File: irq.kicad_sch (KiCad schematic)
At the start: 7 parts, among them U1 74LS85, U11 74HCT00, U18 74LS148, U2 74HCT574, U20 74HCT574, U5 74HCT02

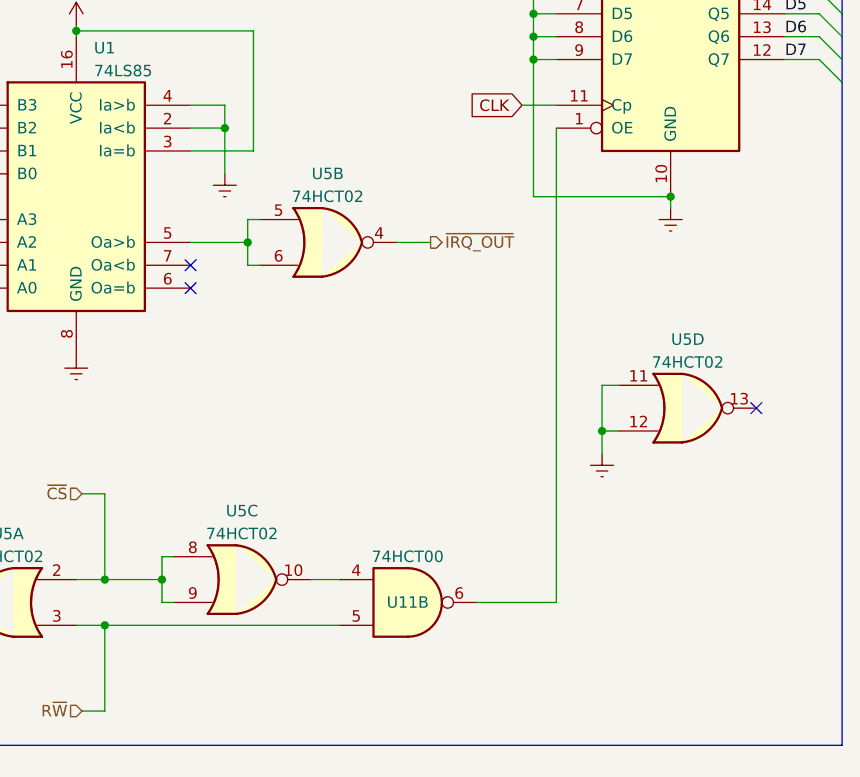
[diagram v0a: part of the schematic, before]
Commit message: fix addrdec design bug, use ca65/cmake instead of vasm/make
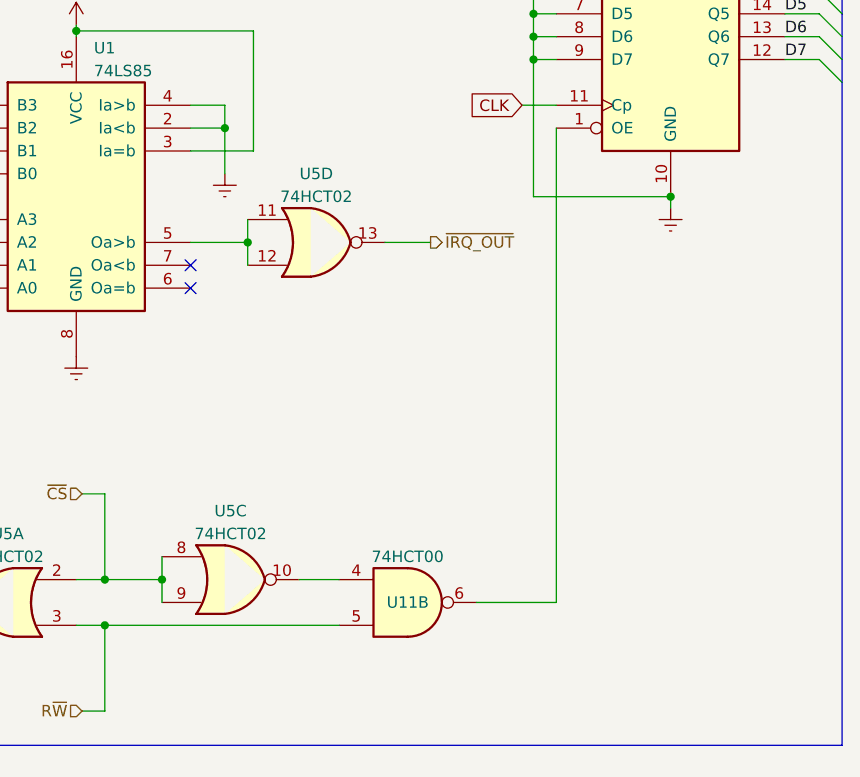
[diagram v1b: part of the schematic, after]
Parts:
- removed unit 4 of U5
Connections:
- net ~{IRQ_OUT}: now also U5.13; no longer U5.4
- new net: U1.5 (Oa>b), U5.11, U5.12
- no-connect marks 8 -> 7
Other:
- moved on the sheet: U5C, U5D

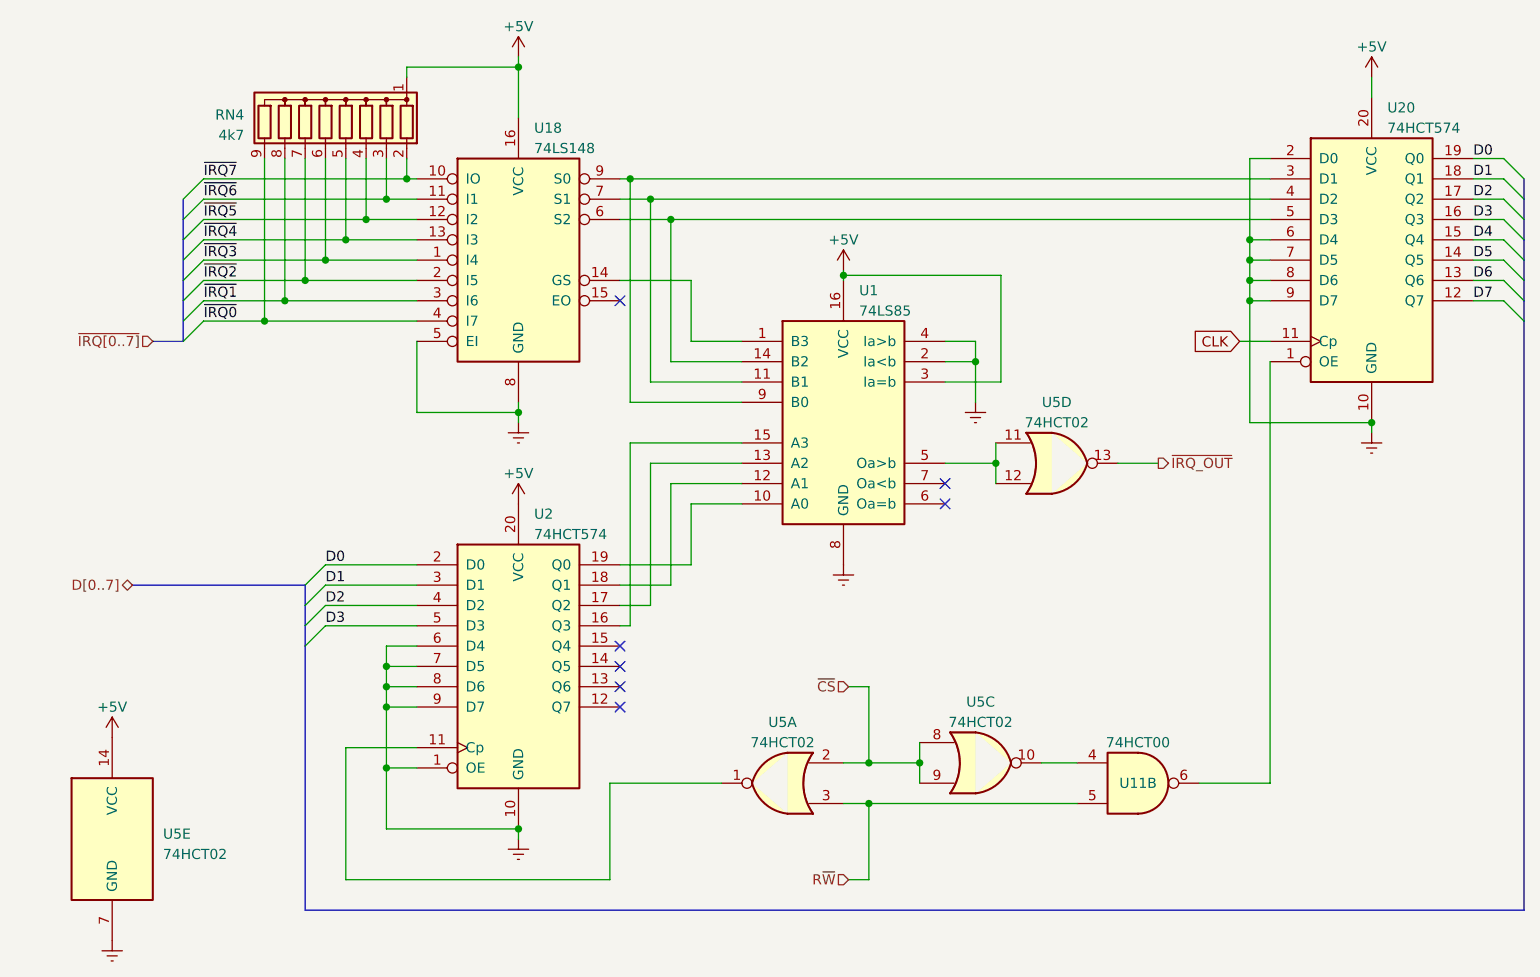
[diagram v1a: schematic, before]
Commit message: add address decoding timings
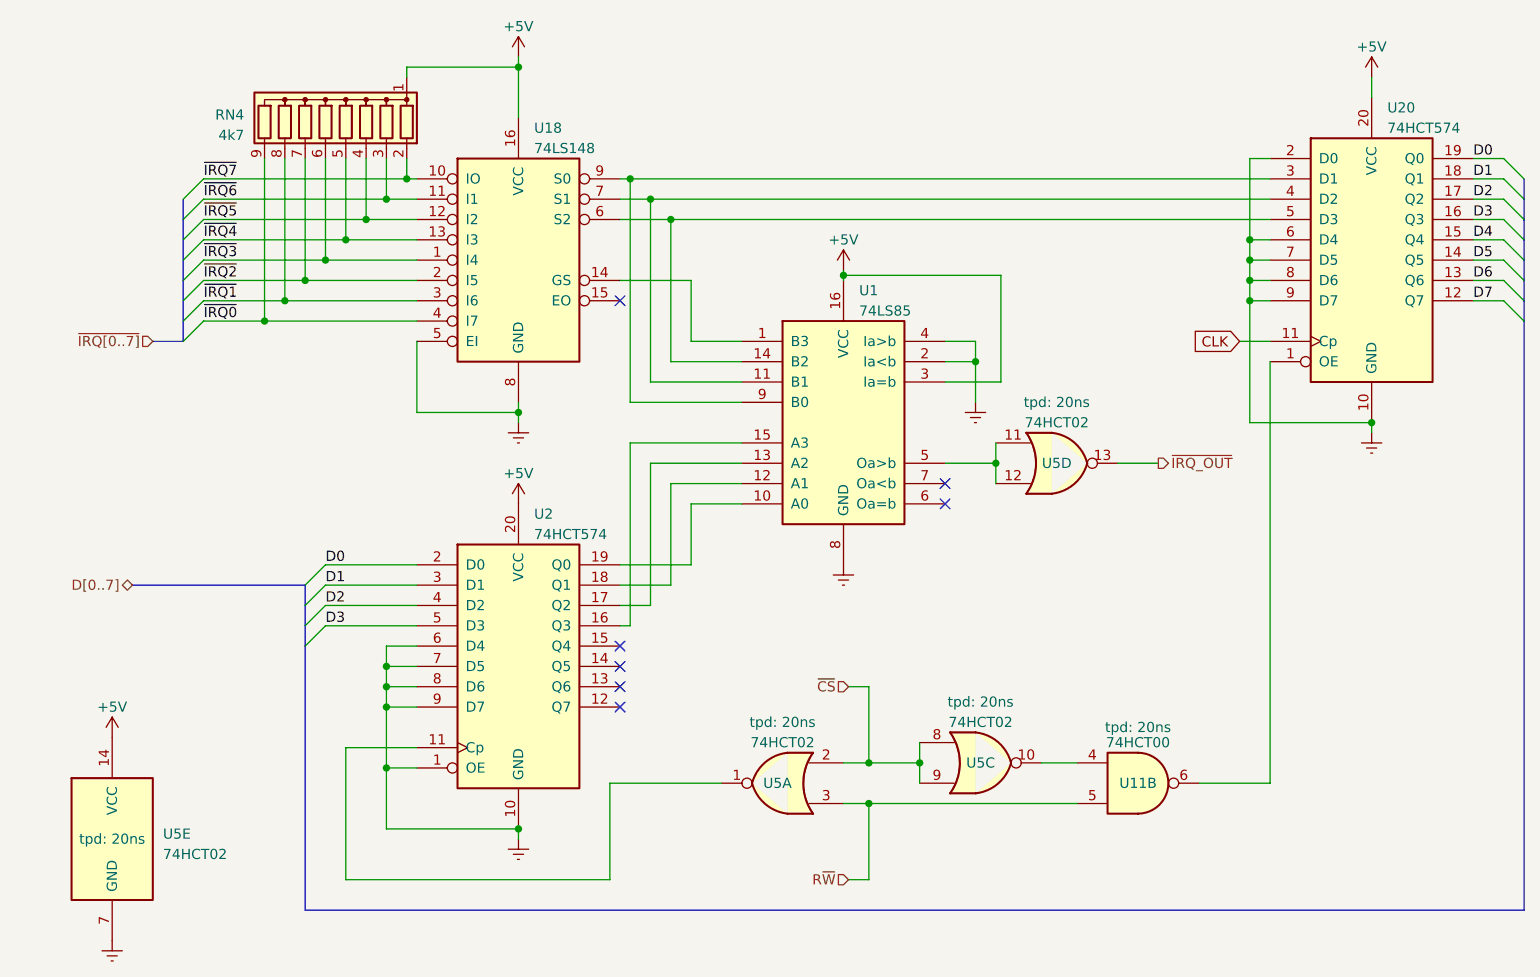
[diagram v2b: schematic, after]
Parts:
- U11, U5: tpd (none) -> 20ns
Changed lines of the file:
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@@
       (effects (font (size 1.27 1.27)) hide)
+    )
+    (property "tpd" "20ns" (at 156.21 105.41 0) (show_name)
+      (effects (font (size 1.27 1.27)))
     )
     (pin "1")
@@
   )
   (symbol (lib_id "74xx:74HCT02") (at 146.05 72.39 0) (unit 4)
-    (in_bom yes) (on_board yes) (dnp no) (fields_autoplaced)
-    (property "Reference" "U5" (at 146.05 64.77 0)
+    (in_bom yes) (on_board yes) (dnp no)
+    (property "Reference" "U5" (at 146.05 72.39 0)
       (effects (font (size 1.27 1.27)))
     )
@@
     (property "Datasheet" "http://www.ti.com/lit/gpn/sn74hct02" (at 146.05 72.39 0)
       (effects (font (size 1.27 1.27)) hide)
+    )
+    (property "tpd" "20ns" (at 146.05 64.77 0) (show_name)
+      (effects (font (size 1.27 1.27)))
     )
     (pin "1")
@@
   )
   (symbol (lib_id "74xx:74HCT02") (at 136.525 109.855 0) (unit 3)
-    (in_bom yes) (on_board yes) (dnp no) (fields_autoplaced)
-    (property "Reference" "U5" (at 136.525 102.235 0)
+    (in_bom yes) (on_board yes) (dnp no)
+    (property "Reference" "U5" (at 136.525 109.855 0)
       (effects (font (size 1.27 1.27)))
     )
@@
     (property "Datasheet" "http://www.ti.com/lit/gpn/sn74hct02" (at 136.525 109.855 0)
       (effects (font (size 1.27 1.27)) hide)
+    )
+    (property "tpd" "20ns" (at 136.525 102.235 0) (show_name)
+      (effects (font (size 1.27 1.27)))
     )
     (pin "1")
@@
       (effects (font (size 1.27 1.27)) hide)
     )
+    (property "tpd" "20ns" (at 27.94 119.38 0) (show_name)
+      (effects (font (size 1.27 1.27)))
+    )
     (pin "1")
     (pin "2")
@@
   )
   (symbol (lib_id "74xx:74HCT02") (at 111.76 112.395 0) (mirror y) (unit 1)
-    (in_bom yes) (on_board yes) (dnp no) (fields_autoplaced)
-    (property "Reference" "U5" (at 111.76 104.775 0)
+    (in_bom yes) (on_board yes) (dnp no)
+    (property "Reference" "U5" (at 111.125 112.395 0)
       (effects (font (size 1.27 1.27)))
     )
@@
       (effects (font (size 1.27 1.27)) hide)
     )
-    (pin "1")
+    (property "tpd" "20ns" (at 111.76 104.775 0) (show_name)
+      (effects (font (size 1.27 1.27)))
+    )
+    (pin "1")

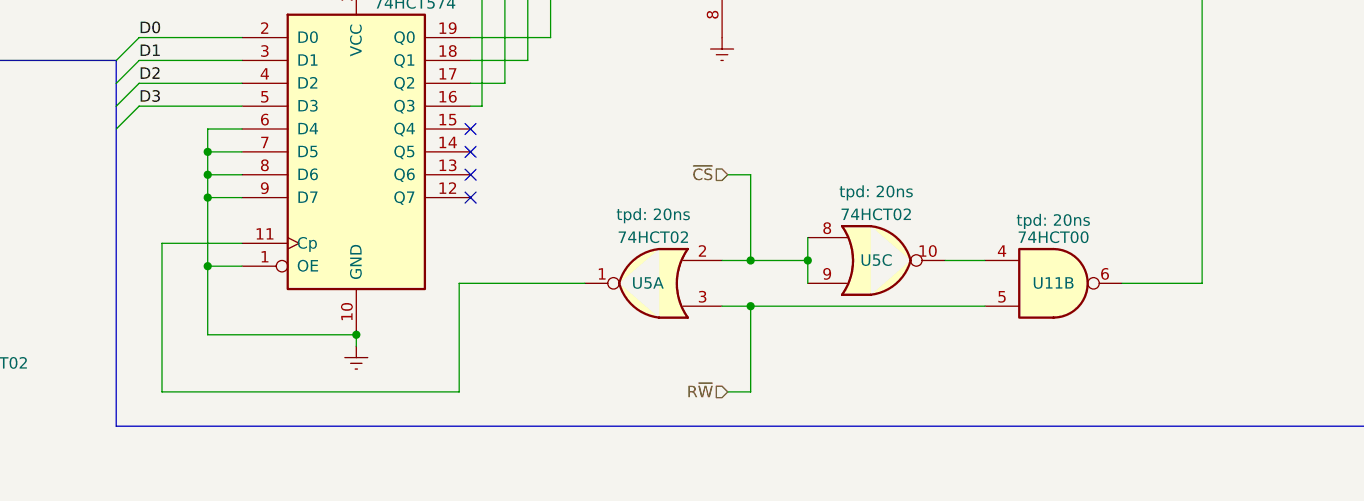
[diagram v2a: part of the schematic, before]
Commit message: fixed bugs in IRQ prio circuit
POST pass
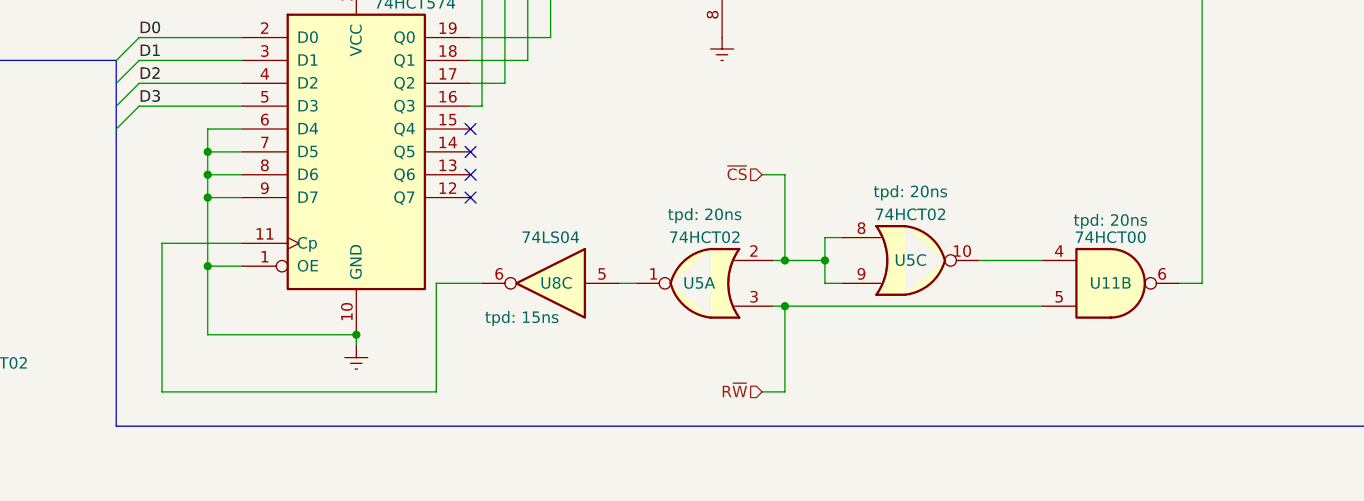
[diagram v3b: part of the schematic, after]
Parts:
- added U8: 74LS04, symbol 74xx:74LS04
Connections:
- net at U2.11 (Cp): now also U8.6; no longer U5.1
- new net: U5.1, U8.5
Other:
- moved on the sheet: U5A, U5C

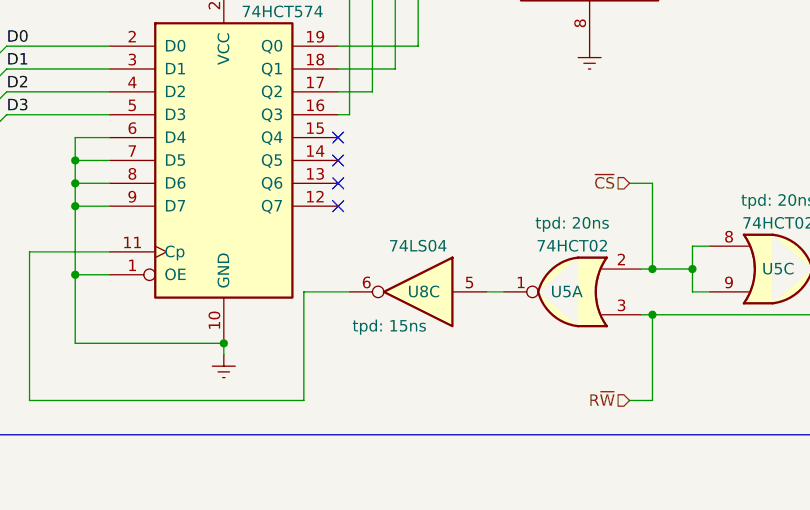
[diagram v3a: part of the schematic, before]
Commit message: output POST status on lcd display
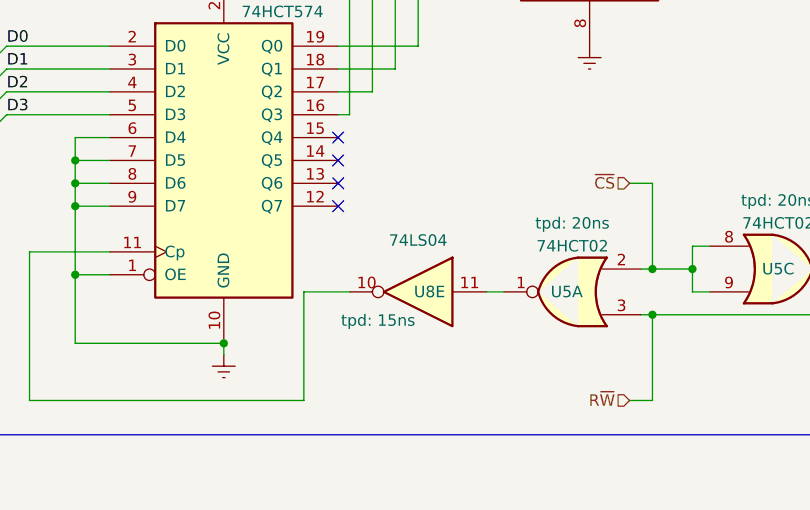
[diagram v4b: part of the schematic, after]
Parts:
- removed U8: 74LS04, symbol 74xx:74LS04
- added U8: 74LS04, symbol 74xx:74LS04
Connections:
- net at U2.11 (Cp): now also U8.10
- net at U5.1: now also U8.11
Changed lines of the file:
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@@
-    )
-  )
-  (symbol (lib_id "74xx:74LS04") (at 100.33 112.395 0) (mirror y) (unit 3)
-    (in_bom yes) (on_board yes) (dnp no)
-    (property "Reference" "U8" (at 100.965 112.395 0)
-      (effects (font (size 1.27 1.27)))
-    )
-    (property "Value" "74LS04" (at 100.33 107.315 0)
-      (effects (font (size 1.27 1.27)))
-    )
-    (property "Footprint" "" (at 100.33 112.395 0)
-      (effects (font (size 1.27 1.27)) hide)
-    )
-    (property "Datasheet" "http://www.ti.com/lit/gpn/sn74LS04" (at 100.33 112.395 0)
-      (effects (font (size 1.27 1.27)) hide)
-    )
-    (property "tpd" "15ns" (at 97.155 116.205 0) (show_name)
-      (effects (font (size 1.27 1.27)))
-    )
-    (pin "1")
-    (pin "2")
-    (pin "3")
-    (pin "4")
-    (pin "5")
-    (pin "6")
-    (pin "8")
-    (pin "9")
-    (pin "10")
-    (pin "11")
-    (pin "12")
-    (pin "13")
-    (pin "14")
-    (pin "7")
-    (instances
-      (project "rod6502"
-        (path "/031ea57b-8d17-4b45-87cc-c58302485ce1/4032fa43-c28c-4c35-b0ce-d5d9da6e84af"
-          (reference "U8") (unit 3)
-        )
-        (path "/031ea57b-8d17-4b45-87cc-c58302485ce1/890f0003-2042-459e-ac4a-1dd81f8fbcc6"
-          (reference "U8") (unit 3)
-        )
-      )
     )
   )
@@
         )
       )
+    )
+  )
+  (symbol (lib_id "74xx:74LS04") (at 100.33 112.395 0) (mirror y) (unit 5)
+    (in_bom yes) (on_board yes) (dnp no)
+    (property "Reference" "U8" (at 101.6 112.395 0)
+      (effects (font (size 1.27 1.27)))
+    )
+    (property "Value" "74LS04" (at 100.33 106.68 0)
+      (effects (font (size 1.27 1.27)))
+    )
+    (property "Footprint" "" (at 100.33 112.395 0)
+      (effects (font (size 1.27 1.27)) hide)
+    )
+    (property "Datasheet" "http://www.ti.com/lit/gpn/sn74LS04" (at 100.33 112.395 0)
+      (effects (font (size 1.27 1.27)) hide)
+    )
+    (property "tpd" "15ns" (at 95.885 115.57 0) (show_name)
+      (effects (font (size 1.27 1.27)))
+    )
+    (pin "1")
+    (pin "2")
+    (pin "3")
+    (pin "4")
+    (pin "5")
+    (pin "6")
+    (pin "8")
+    (pin "9")
+    (pin "10")
+    (pin "11")
+    (pin "12")
+    (pin "13")
+    (pin "14")
+    (pin "7")
+    (instances
+      (project "rod6502"
+        (path "/031ea57b-8d17-4b45-87cc-c58302485ce1/4032fa43-c28c-4c35-b0ce-d5d9da6e84af"
+          (reference "U8") (unit 5)
+        )
+        (path "/031ea57b-8d17-4b45-87cc-c58302485ce1/890f0003-2042-459e-ac4a-1dd81f8fbcc6"
+          (reference "U8") (unit 5)
+        )
+      )

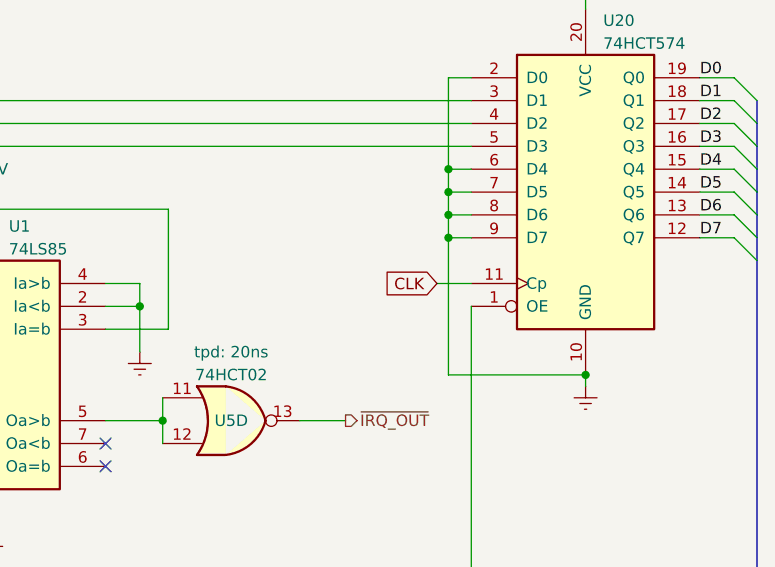
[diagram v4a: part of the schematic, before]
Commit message: RS-232/ACIA works!
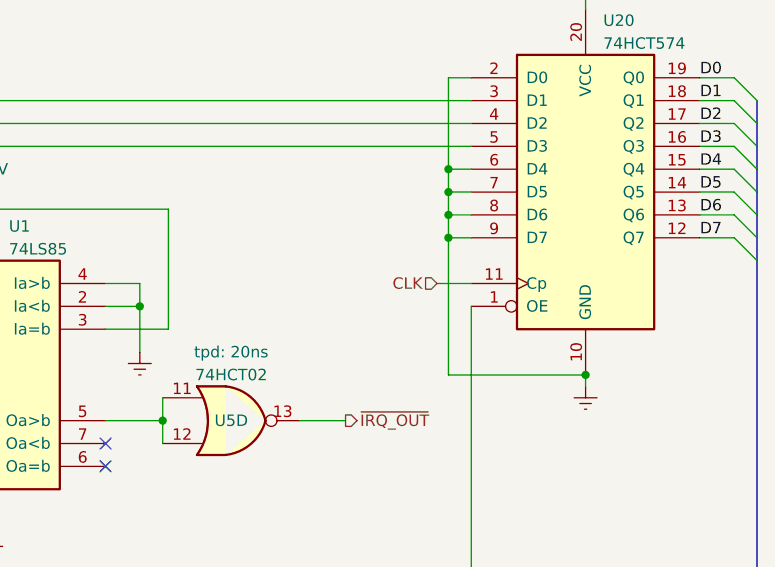
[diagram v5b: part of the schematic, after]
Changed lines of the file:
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@@
     (effects (font (size 1.27 1.27)) (justify left bottom))
-  )
-  (global_label "CLK" (shape input) (at 168.91 57.15 180) (fields_autoplaced)
-    (effects (font (size 1.27 1.27)) (justify right))
-    (property "Intersheetrefs" "${INTERSHEET_REFS}" (at 162.4361 57.15 0)
-      (effects (font (size 1.27 1.27)) (justify right) hide)
-    )
   )
   (hierarchical_label "~{CS}" (shape input) (at 123.825 100.33 180) (fields_autoplaced)
@@
     )
   )
+  (hierarchical_label "CLK" (shape input) (at 168.91 57.15 180) (fields_autoplaced)
+    (effects (font (size 1.27 1.27)) (justify right))
+  )
   (hierarchical_label "~{IRQ_OUT}" (shape output) (at 158.75 72.39 0) (fields_autoplaced)
